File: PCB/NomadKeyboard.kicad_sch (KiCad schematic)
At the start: 90 parts, among them J1 4PIN, SW1 SW_PUSH_LED, SW10 SW_PUSH_LED, SW11 SW_PUSH_LED, SW12 SW_PUSH_LED, SW13 SW_PUSH_LED, SW14 SW_PUSH_LED, SW15 SW_PUSH_LED, SW16 SW_PUSH_LED, SW17 SW_PUSH_LED, SW18 SW_PUSH_LED, SW19 SW_PUSH_LED, SW2 SW_PUSH_LED, SW20 SW_PUSH_LED, SW21 SW_PUSH_LED, SW22 SW_PUSH_LED, SW23 SW_PUSH_LED, SW24 SW_PUSH_LED, SW25 SW_PUSH_LED, SW26 SW_PUSH_LED, SW27 SW_PUSH_LED, SW28 SW_PUSH_LED, SW29 SW_PUSH_LED, SW3 SW_PUSH_LED, SW30 SW_PUSH_LED, SW31 SW_PUSH_LED, SW32 SW_PUSH_LED, SW33 SW_PUSH_LED, SW34 SW_PUSH_LED, SW35 SW_PUSH_LED, SW36 SW_PUSH_LED, SW37 SW_PUSH_LED, SW38 SW_PUSH_LED, SW39 SW_PUSH_LED, SW4 SW_PUSH_LED, SW40 SW_PUSH_LED, SW41 SW_PUSH_LED, SW42 RotaryEncoder_Switch, SW5 SW_PUSH_LED, SW6 SW_PUSH_LED, SW7 SW_PUSH_LED, SW8 SW_PUSH_LED, SW9 SW_PUSH_LED, U1 RP2040

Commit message: new design wip
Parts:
- removed J_RGB1: RGB jumper, Jumper:SolderJumper-3_P2.0mm_Open_TrianglePad1.0x1.5mm, symbol Jumper:Jumper_3_Open
- removed SW42: RotaryEncoder_Switch, Rotary_Encoder:RotaryEncoder_Alps_EC11E-Switch_Vertical_H20mm, symbol Device:RotaryEncoder_Switch
- added D44, D45, D48, D49, D50, D51, D52, D53, D54, D55, D56, D57, D58, D59, D60: D, SofleChoc:crkbd-diode, symbol SofleKeyboard-rescue:D-Lily58-cache-Lily58_Pro-rescue
- added JP1, JP2: Hand select, Jumper:SolderJumper-2_P1.3mm_Open_RoundedPad1.0x1.5mm, symbol Jumper:SolderJumper_2_Open
- added SW44, SW45, SW48, SW49, SW50, SW51, SW52, SW53, SW54, SW55, SW56, SW57, SW58, SW59, SW60: SW_PUSH_LED, SofleChoc:Choc_Hotswap_SK6812MiniE, symbol SofleKeyboard:SW_PUSH_LED
- U1: footprint RP2040:RP2040-mini -> SofleChoc:ProMicro
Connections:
- net enc_d is gone; now on net LED: U1.14 (D16(PB2))
- net enc_i is gone; now on net COL6: U1.13 (D10(PB6))
- net enc_s is gone; now on net COL8: U1.16 (D15(PB1))
- net COL0: now also SW54.6
- net COL1: now also SW53.6
- net COL2: now also SW52.6
- net COL3: now also SW51.6
- net COL4: now also SW50.6
- net COL5: now also U1.12 (D9(PB5)), SW49.6; no longer U1.9 (D6(PD7))
- net COL6: now also SW45.6, SW48.6; no longer SW22.6, U1.10 (D7(PE6))
- net COL7: now also SW22.6
- net COL8: now also SW44.6; no longer U1.12 (D9(PB5))
- net DATA: now also U1.1 (TX(PD3)); no longer U1.22 (RST)
- net GND: now also U1.23 (GND), U1.3 (GND), JP1.2 (B), SW44.3 (GND), SW45.3 (GND), SW48.3 (GND), SW49.3 (GND), SW50.3 (GND), SW51.3 (GND), SW52.3 (GND), SW53.3 (GND), SW54.3 (GND), SW55.3 (GND), SW56.3 (GND), SW57.3 (GND), SW58.3 (GND), SW59.3 (GND), SW60.3 (GND); no longer U1.2 (RX(PD2))
- net LED: now also SW55.4 (DIN); no longer U1.23 (GND)
- net ROW0: now also U1.2 (RX(PD2)), D55.1 (K); no longer U1.21 (VCC)
- net ROW1: now also D56.1 (K)
- net ROW2: now also D57.1 (K)
- net ROW3: now also D44.1 (K), D45.1 (K), D58.1 (K); no longer D22.1 (K)
- net ROW4: now also D22.1 (K), D59.1 (K)
- net VCC: now also U1.21 (VCC), JP2.2 (B), SW44.1 (VDD), SW45.1 (VDD), SW48.1 (VDD), SW49.1 (VDD), SW50.1 (VDD), SW51.1 (VDD), SW52.1 (VDD), SW53.1 (VDD), SW54.1 (VDD), SW55.1 (VDD), SW56.1 (VDD), SW57.1 (VDD), SW58.1 (VDD), SW59.1 (VDD), SW60.1 (VDD); no longer U1.3 (GND)
- net led_bridge: no longer SW34.2 (DOUT)
- net HAND: now reaches U1.15 (D14(PB3))
- net HAND: now also JP1.1 (A), JP2.1 (A)
- net at SW15.2 (DOUT): now also SW45.4 (DIN); no longer SW38.4 (DIN)
- net at SW22.4 (DIN): now also SW44.2 (DOUT); no longer SW38.2 (DOUT)
- net LED_start: no longer names the net of SW41.4 (DIN)
- net LED_start: now also SW48.2 (DOUT)
- new net: SW34.2 (DOUT), SW60.4 (DIN)
- new net: D48.2 (A), SW48.5
- new net: D55.2 (A), SW55.5
- new net: D50.2 (A), SW50.5
- new net: D56.2 (A), SW56.5
- new net: SW51.4 (DIN), SW52.2 (DOUT)
- new net: SW52.4 (DIN), SW53.2 (DOUT)
- new net: D57.2 (A), SW57.5
- new net: SW57.4 (DIN), SW58.2 (DOUT)
- new net: SW58.4 (DIN), SW59.2 (DOUT)
- new net: D51.2 (A), SW51.5
- new net: D52.2 (A), SW52.5
- new net: SW48.4 (DIN), SW49.2 (DOUT)
- new net: SW38.4 (DIN), SW45.2 (DOUT)
- new net: D45.2 (A), SW45.5
- new net: D49.2 (A), SW49.5
- new net: SW38.2 (DOUT), SW44.4 (DIN)
- new net: SW56.4 (DIN), SW57.2 (DOUT)
- new net: D53.2 (A), SW53.5
- new net: D60.2 (A), SW60.5
- new net: SW53.4 (DIN), SW54.2 (DOUT)
- new net: D44.2 (A), SW44.5
- new net: SW50.4 (DIN), SW51.2 (DOUT)
- new net: D59.2 (A), SW59.5
- new net: SW49.4 (DIN), SW50.2 (DOUT)
- new net: D58.2 (A), SW58.5
- new net: SW59.4 (DIN), SW60.2 (DOUT)
- new net: D54.2 (A), SW54.5
- new net: SW54.4 (DIN), SW55.2 (DOUT)
- new net COL9: SW55.6, SW56.6, SW57.6, SW58.6, SW59.6, SW60.6, U1.10 (D7(PE6))
- new net ROW5: D48.1 (K), D49.1 (K), D50.1 (K), D51.1 (K), D52.1 (K), D53.1 (K), D54.1 (K), D60.1 (K), U1.9 (D6(PD7))
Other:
- moved on the sheet: D1, D10, D11, D12, D13, D14, D15, D16, D17, D18, D19, D2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

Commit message: new design wip
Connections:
- net LED: now also SW48.4 (DIN); no longer SW55.4 (DIN)
- net ROW0: now also D56.1 (K); no longer D55.1 (K)
- net ROW1: now also D57.1 (K); no longer D56.1 (K)
- net ROW2: now also D58.1 (K); no longer D57.1 (K)
- net ROW3: now also D59.1 (K); no longer D58.1 (K)
- net ROW4: now also D60.1 (K); no longer D59.1 (K)
- net ROW5: now also D55.1 (K); no longer D60.1 (K)
- net at SW3.4 (DIN): now also SW50.2 (DOUT); no longer SW2.2 (DOUT)
- net at SW4.2 (DOUT): now also SW51.4 (DIN); no longer SW5.4 (DIN)
- net at SW6.2 (DOUT): now also SW53.4 (DIN); no longer SW7.4 (DIN)
- net at SW52.2 (DOUT): now also SW5.4 (DIN); no longer SW51.4 (DIN)
- net at SW52.4 (DIN): now also SW51.2 (DOUT); no longer SW53.2 (DOUT)
- net at SW49.2 (DOUT): now also SW50.4 (DIN); no longer SW48.4 (DIN)
- net at SW56.2 (DOUT): now also SW55.4 (DIN)
- net at SW54.2 (DOUT): now also SW7.4 (DIN); no longer SW53.4 (DIN)
- net at SW49.4 (DIN): now also SW2.2 (DOUT); no longer SW50.2 (DOUT)
- net at SW54.4 (DIN): now also SW53.2 (DOUT); no longer SW55.2 (DOUT)
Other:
- moved on the sheet: D55, D56, D57, D58, D59, D60, SW10B, SW11B, SW12B, SW13B, SW14B, SW15B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

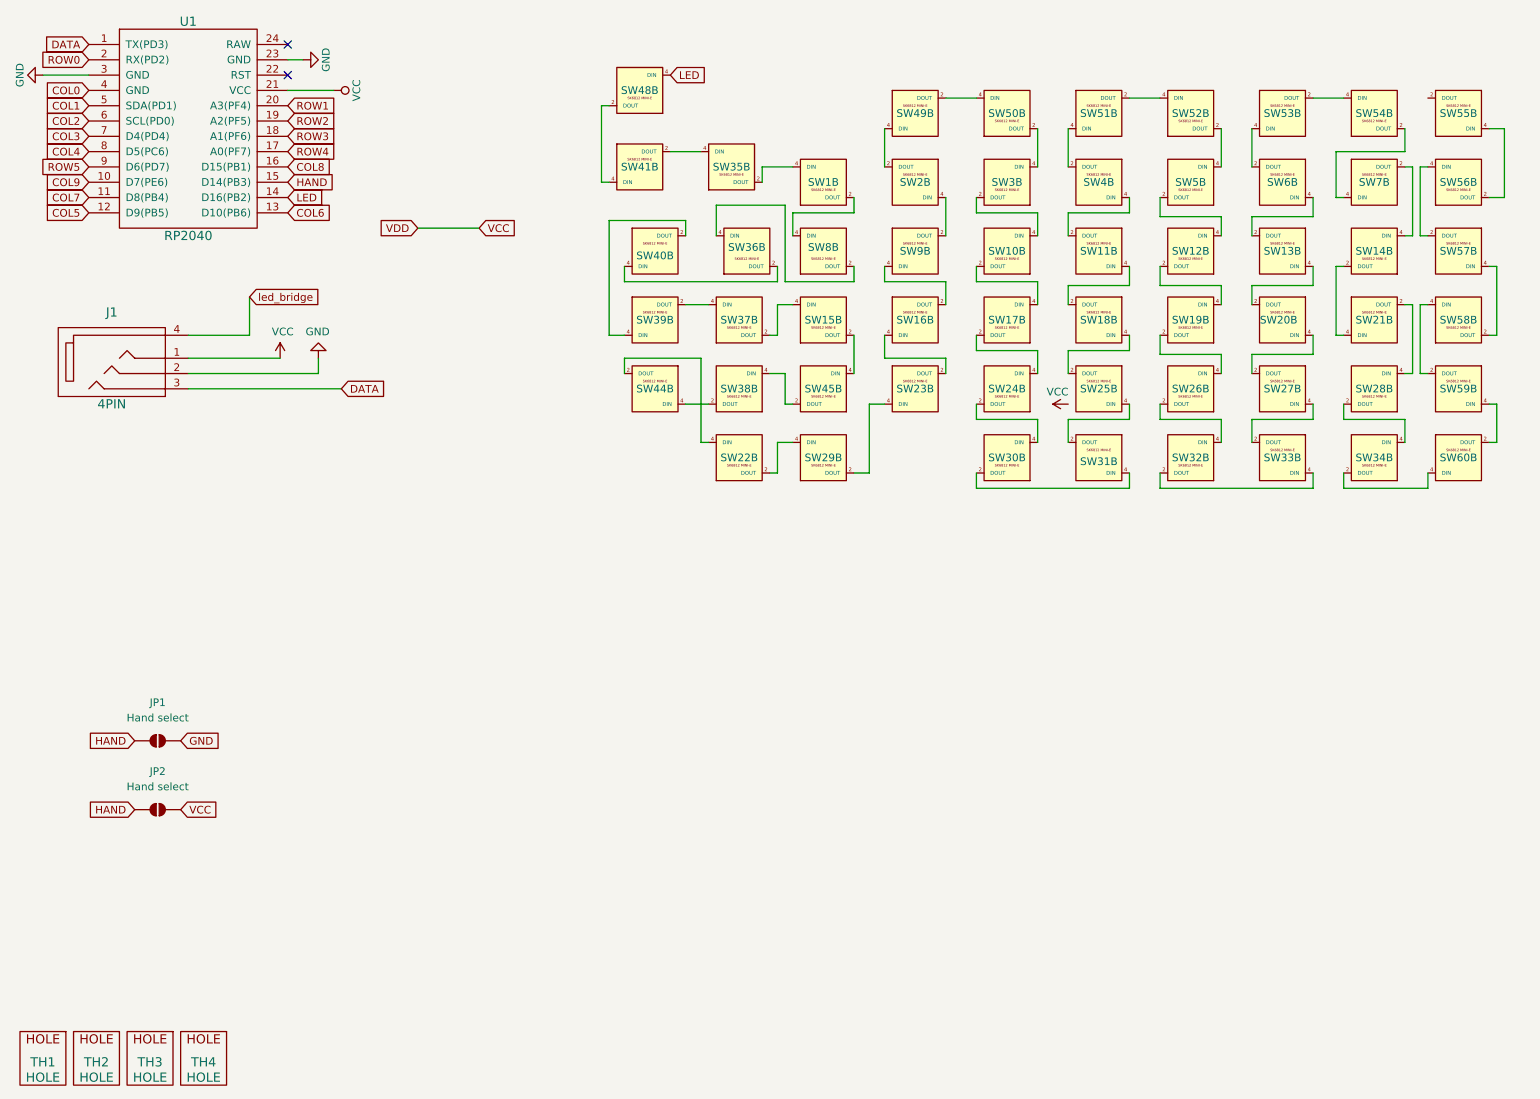
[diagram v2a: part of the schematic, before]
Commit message: added rp2040
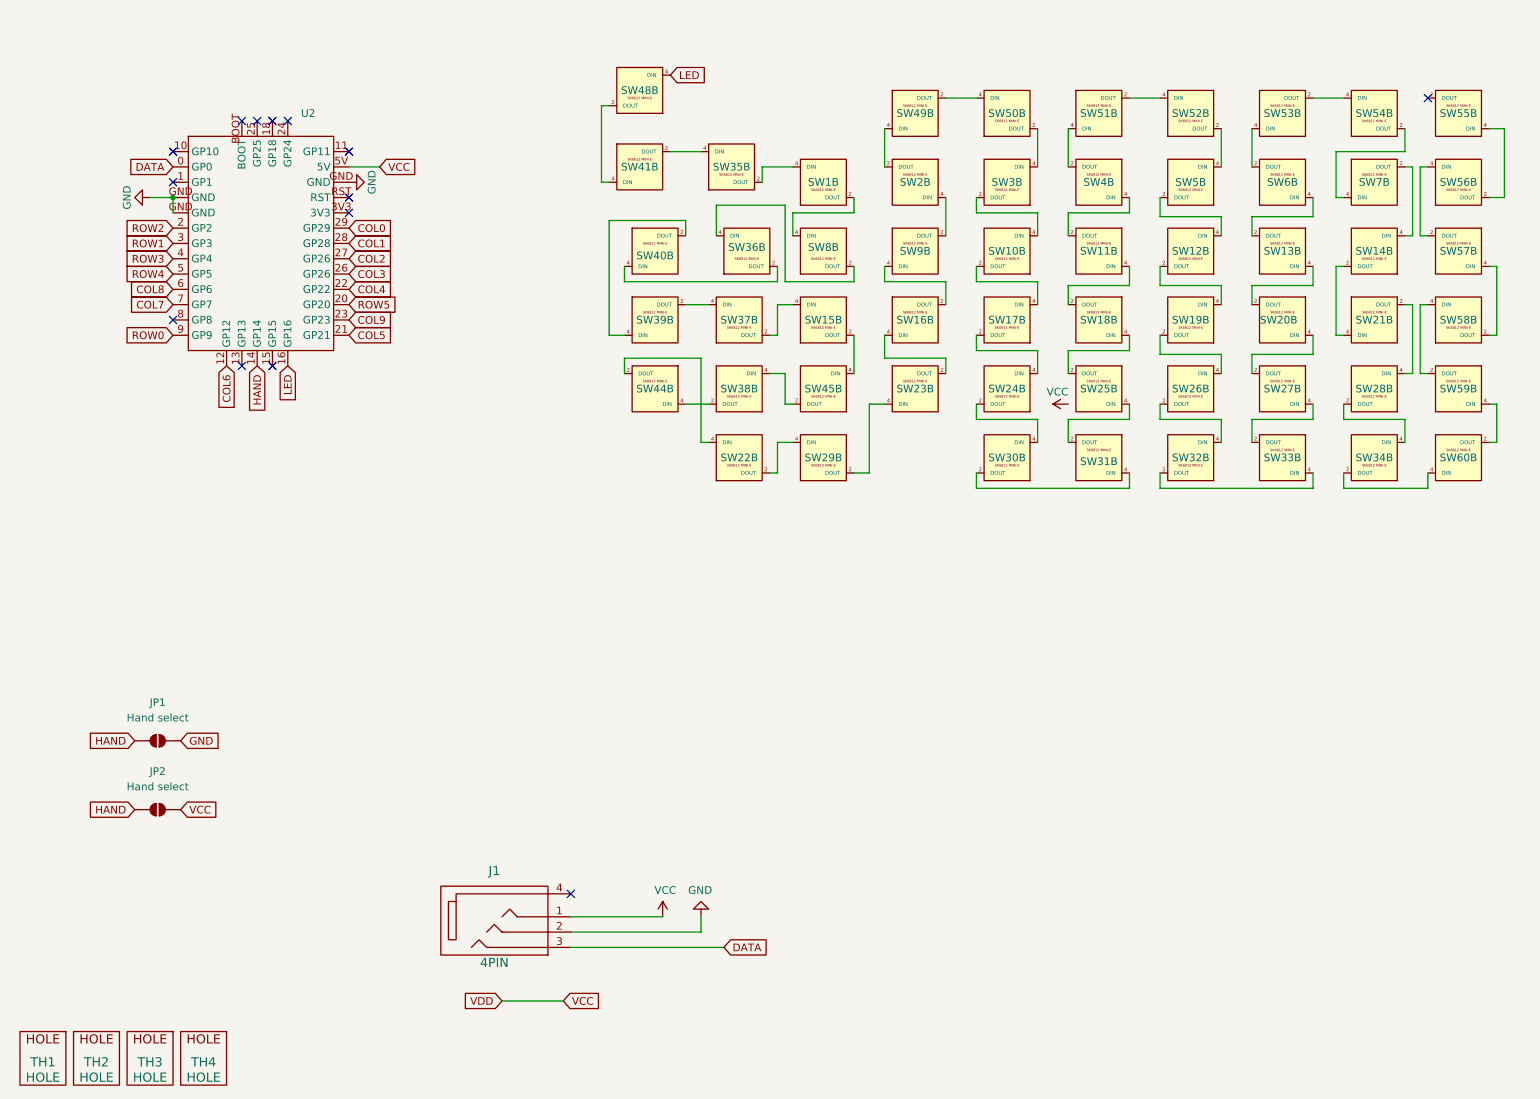
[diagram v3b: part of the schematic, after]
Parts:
- removed U1: RP2040, SofleChoc:ProMicro, symbol SofleKeyboard-rescue:ProMicro_2-Lily58-cache-Lily58_Pro-rescue
- added U2: ~, SofleChoc:pro_micro_rp2040, symbol Sofle:pro_micro_rp2040
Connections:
- net COL0: now also U2.29 (GP29)
- net COL1: now also U2.28 (GP28)
- net COL2: now also U2.27 (GP26)
- net COL3: now also U2.26 (GP26)
- net COL4: now also U2.22 (GP22)
- net COL5: now also U2.21 (GP21)
- net COL6: now also U2.12 (GP12)
- net COL7: now also U2.7 (GP7)
- net COL8: now also U2.6 (GP6)
- net COL9: now also U2.23 (GP23)
- net DATA: now also U2.0 (GP0)
- net GND: now also U2.GND
- net HAND: now also U2.14 (GP14)
- net LED: now also U2.16 (GP16)
- net ROW0: now also U2.9 (GP9)
- net ROW1: now also U2.3 (GP3)
- net ROW2: now also U2.2 (GP2)
- net ROW3: now also U2.4 (GP4)
- net ROW4: now also U2.5 (GP5)
- net ROW5: now also U2.20 (GP20)
- net VCC: now also U2.5V
- net led_bridge: no longer names the net of J1.4
- no-connect marks 2 -> 14
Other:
- moved on the sheet: J1
